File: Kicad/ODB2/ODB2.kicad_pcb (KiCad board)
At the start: 4 copper layers, 83.9 x 76.5 mm, 184 parts, among them J4 RF2-04A-T-00-50-G, J5 RFM_Conn_Coaxial, U1 STM32F412ZGTx, U10 W25Q512JVEIQ, U5 L76L-M33, U6 ICM-20948, U7 MS580301BA01-00

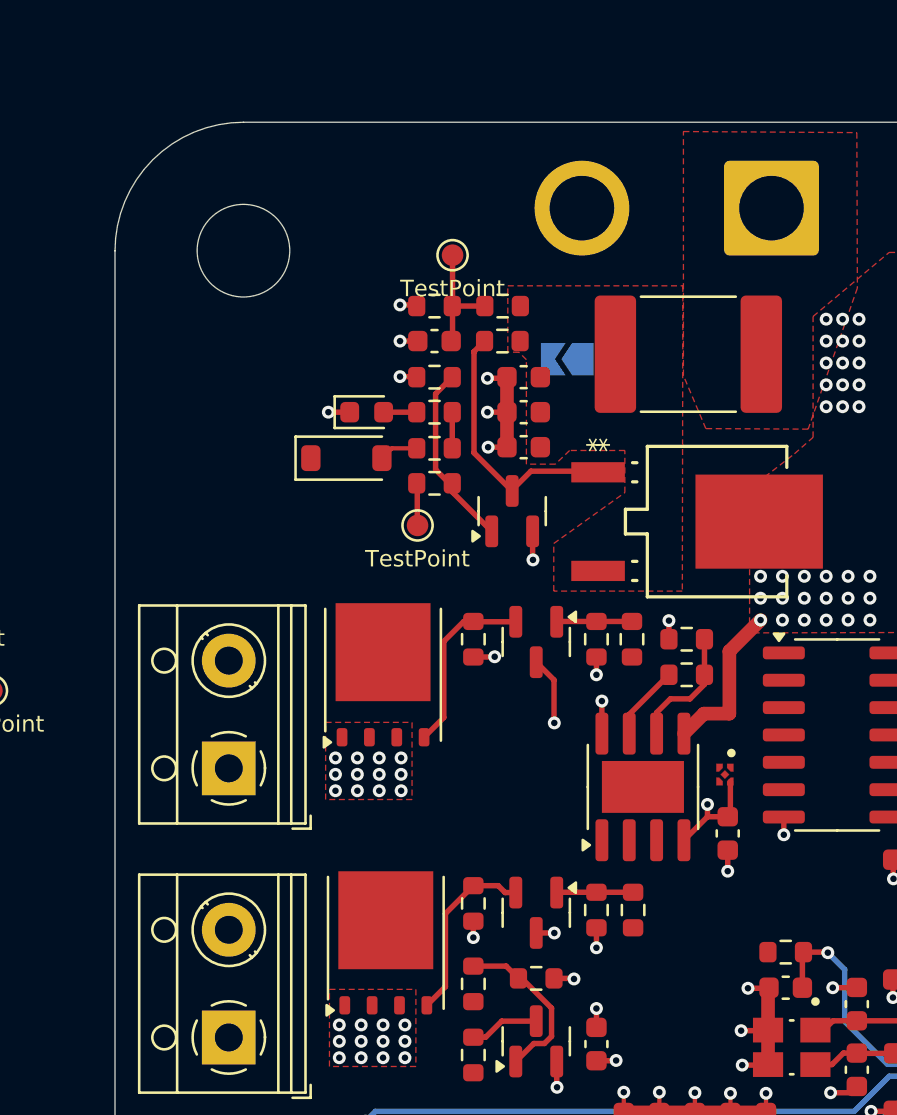
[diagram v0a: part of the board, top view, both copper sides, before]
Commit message: Changed XNOR Gate and OP AMP to 1 chanel
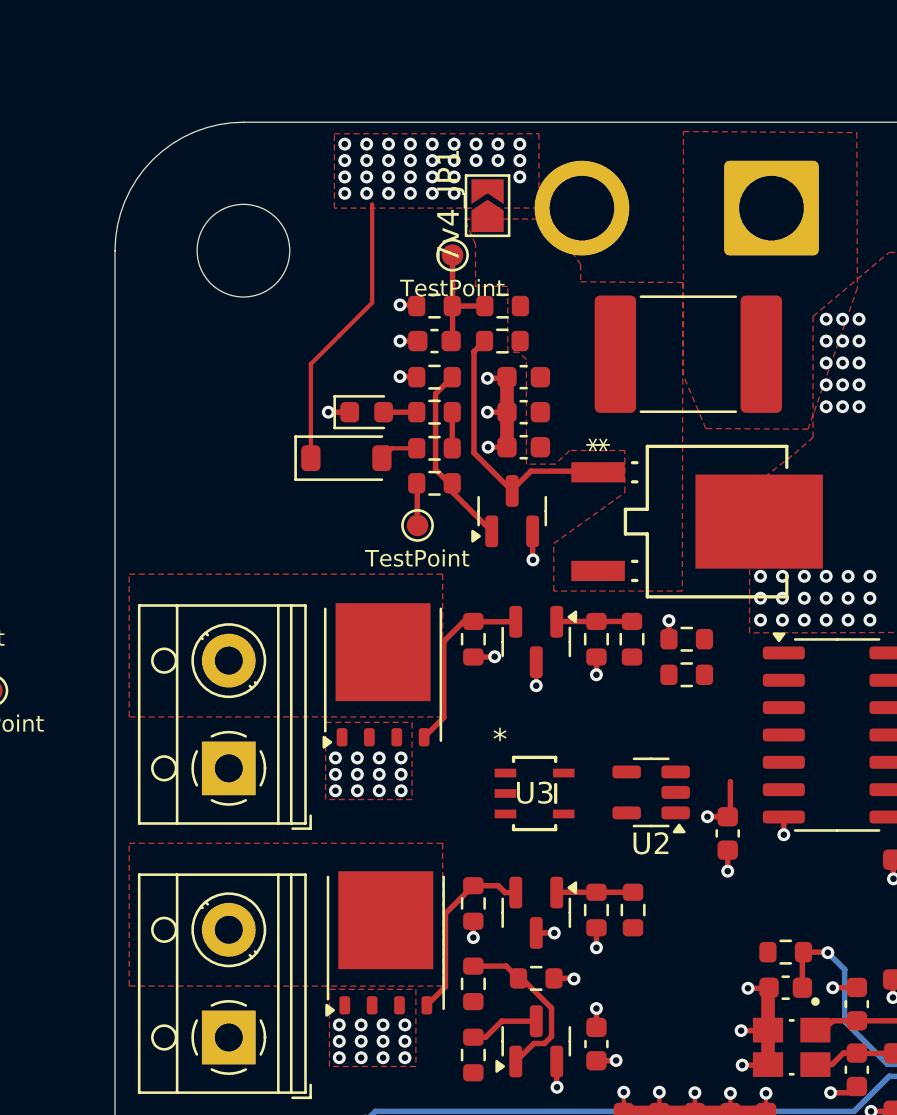
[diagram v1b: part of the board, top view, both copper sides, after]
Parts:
- removed Pyros_AMP1: TLV2372, Package_SO:SOIC-8-1EP_3.9x4.9mm_P1.27mm_EP2.41x3.81mm
- removed Pyros_XNOR1: 74LV1T87GXH, Library:IC_74LV1T87GXH
- added U2: TLV2371DBV, Package_TO_SOT_SMD:SOT-23-5, F.Cu at (24.9, 31.1)
- added U3: 74LV1T87GVH, ODB:SC-74A_SOT753_NEX, F.Cu at (19.5, 31.2)
- 7v4_JP1: moved to F.Cu
- moved 7v4_JP1 8.03 mm to (17.3, 3.87), turned to 90 degrees
- turned Pyros_R4 to 180 degrees
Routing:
- net Net-(U2--): track 5.84 -> 0.00 mm
- net +7V4: track 7.44 -> 13.0 mm, vias 33 -> 64
- net +3V3: track 103.2 -> 99.0 mm
- net Pyros_MainADC: track 3.49 -> 0.00 mm
- net GND: track 155.0 -> 153.4 mm, vias 150 -> 149
- added copper zone on F.Cu, net Net-(Pyros_J1-Pin_2)
- added copper zone on F.Cu, net Net-(Pyros_J2-Pin_2)

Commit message: Updated pcb
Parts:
- removed TP16: TestPoint, TestPoint:TestPoint_Pad_D1.0mm
- Boot_JP1: moved to F.Cu
- moved TP23 45.4 mm to (33.2, 34.2)
- moved TP15 34.6 mm to (28.9, 25.8)
- moved TP22 29.8 mm to (18.0, 33.6)
- moved TP12 27.4 mm to (14.6, 46.2)
- moved TP8 16.4 mm to (72.3, 27.0)
- moved TP7 16.1 mm to (74.6, 27.1)
- moved U3 7.99 mm to (27.1, 28.8)
- moved U2 3.71 mm to (22.0, 28.8)
- moved J5 1.57 mm to (18.5, 69.0)
- moved J4 1.39 mm to (79.3, 43.9)
- moved TP4 0.71 mm to (25.7, 54.8)
- moved Boot_JP1 0.67 mm to (45.2, 24.9)
- moved TP31 0.66 mm to (54.5, 6.88)
- moved TP3 0.61 mm to (23.4, 54.8)
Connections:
- U1 pad 45: Pyros_DrogueADC -> unconnected-(U1-PC5-Pad45)
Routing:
- net Pyros_MainOn: track 0.00 -> 93.1 mm, vias 0 -> 3
- net 7v4_An: track 5.54 -> 58.9 mm, vias 0 -> 2
- net Pyros_MainADC: track 0.00 -> 46.8 mm, vias 0 -> 4
- net 7v4Enable: track 1.96 -> 44.9 mm, vias 0 -> 3
- net SPI5_Mem_MOSI: track 1.92 -> 42.9 mm, vias 0 -> 2
- net Buzzer_PWM: track 0.00 -> 40.6 mm
- net ~Pyros_Test: track 0.00 -> 39.5 mm, vias 0 -> 4
- net SPI4_Baro_CS: track 4.19 -> 36.0 mm, vias 0 -> 2
- net SPI5_Mem_MISO: track 3.23 -> 30.8 mm, vias 0 -> 2
- net ICM_INT: track 3.66 -> 28.7 mm, vias 2 -> 3
- net Pyros_DrogueOn: track 0.00 -> 24.6 mm
- net Pyros_Bluetooth: track 0.00 -> 24.2 mm
- net Pyros_DrogueODB: track 0.00 -> 21.9 mm, vias 0 -> 2
- net +7V4: track 13.0 -> 34.3 mm
- net Pyros_MainODB: track 0.00 -> 20.0 mm, vias 0 -> 2
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
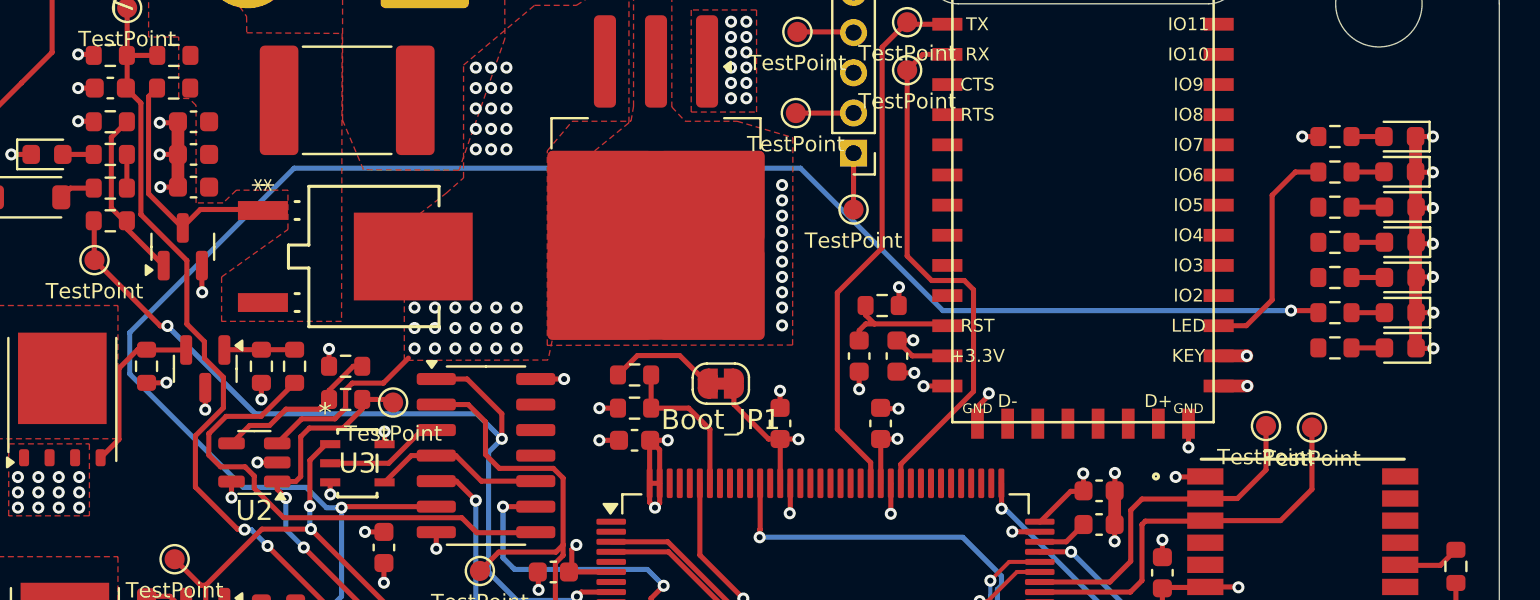
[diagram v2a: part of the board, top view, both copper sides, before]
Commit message: pcb fixes leds
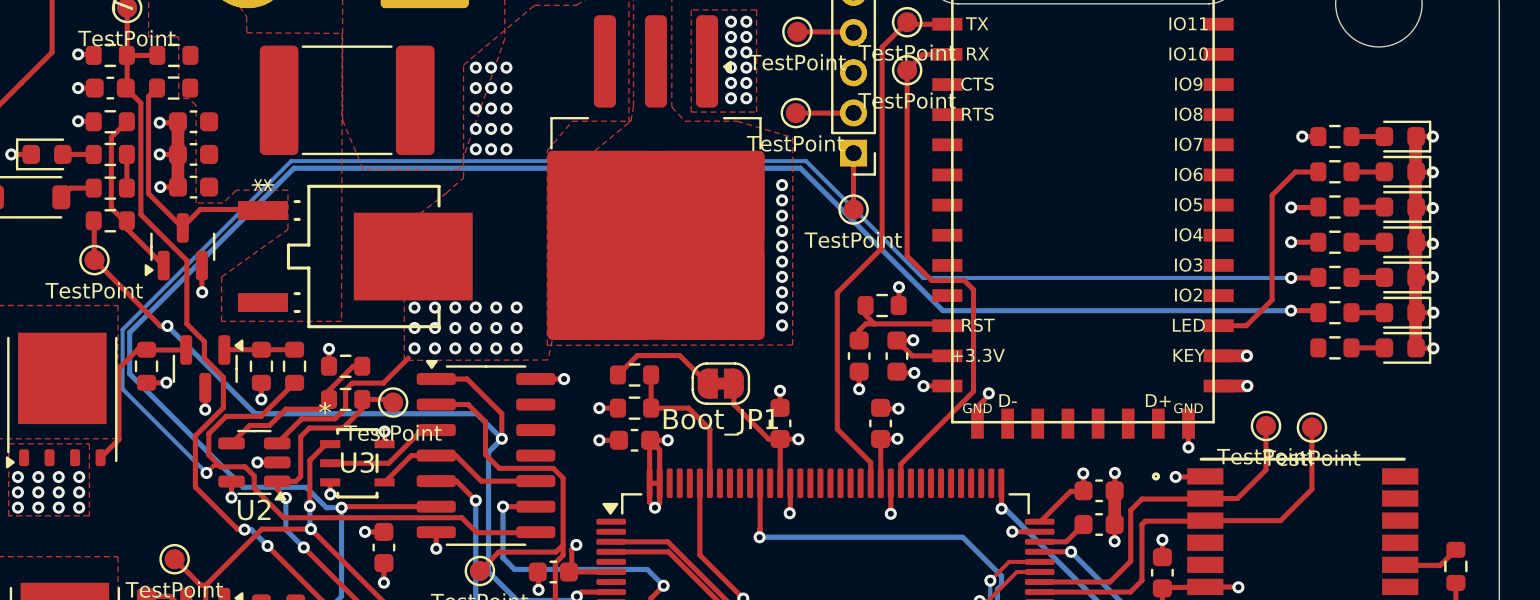
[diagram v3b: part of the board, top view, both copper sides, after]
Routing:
- net Pyros_DrogueOn: track 24.6 -> 99.6 mm, vias 0 -> 2
- net 7v4Enable: track 44.9 -> 46.2 mm, vias 3 -> 4
- net Pyros_Bluetooth: track 24.2 -> 25.4 mm, vias 0 -> 1
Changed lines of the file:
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@@
 		(tags "net tie solder jumper bridged")
 		(property "Reference" "Boot_JP1"
-			(at 0 -1.8 360)
+			(at 0 -1.8 0)
 			(layer "F.SilkS")
 			(effects
@@
 		)
 		(property "Value" "SolderJumper_2_Open"
-			(at 0 1.9 360)
+			(at 0 1.9 0)
 			(layer "F.Fab")
 			(effects
@@
 	(footprint "LED_SMD:LED_0603_1608Metric"
 		(layer "F.Cu")
-		(at 78.9941 14.3256 180)
+		(at 79.0194 14.3256 180)
 		(descr "LED SMD 0603 (1608 Metric), square (rectangular) end terminal, IPC_7351 nominal, (Body size source: http://www.tortai-tech.com/upload/download/2011102023233369053.pdf), generated with kicad-footprint-generator")
 		(tags "LED")
@@
 	(footprint "Resistor_SMD:R_0603_1608Metric"
 		(layer "F.Cu")
-		(at 75.7683 21.336 180)
+		(at 75.7682 21.336 180)
 		(descr "Resistor SMD 0603 (1608 Metric), square (rectangular) end terminal, IPC_7351 nominal, (Body size source: IPC-SM-782 page 72, https://www.pcb-3d.com/wordpress/wp-content/uploads/ipc-sm-782a_amendment_1_and_2.pdf), generated with kicad-footprint-generator")
 		(tags "resistor")
@@
 	(footprint "LED_SMD:LED_0603_1608Metric"
 		(layer "F.Cu")
-		(at 79.0195 16.0782 180)
+		(at 79.0194 16.0782 180)
 		(descr "LED SMD 0603 (1608 Metric), square (rectangular) end terminal, IPC_7351 nominal, (Body size source: http://www.tortai-tech.com/upload/download/2011102023233369053.pdf), generated with kicad-footprint-generator")
 		(tags "LED")
@@
 	(footprint "LED_SMD:LED_0603_1608Metric"
 		(layer "F.Cu")
-		(at 78.9941 12.573 180)
+		(at 79.0194 12.573 180)
 		(descr "LED SMD 0603 (1608 Metric), square (rectangular) end terminal, IPC_7351 nominal, (Body size source: http://www.tortai-tech.com/upload/download/2011102023233369053.pdf), generated with kicad-footprint-generator")
 		(tags "LED")
@@
 	(footprint "Resistor_SMD:R_0603_1608Metric"
 		(layer "F.Cu")
-		(at 75.7683 16.087)
+		(at 75.7682 16.0782)
 		(descr "Resistor SMD 0603 (1608 Metric), square (rectangular) end terminal, IPC_7351 nominal, (Body size source: IPC-SM-782 page 72, https://www.pcb-3d.com/wordpress/wp-content/uploads/ipc-sm-782a_amendment_1_and_2.pdf), generated with kicad-footprint-generator")
 		(tags "resistor")
@@
 	(footprint "LED_SMD:LED_0603_1608Metric"
 		(layer "F.Cu")
-		(at 79.0195 17.8308 180)
+		(at 79.0194 17.8308 180)
 		(descr "LED SMD 0603 (1608 Metric), square (rectangular) end terminal, IPC_7351 nominal, (Body size source: http://www.tortai-tech.com/upload/download/2011102023233369053.pdf), generated with kicad-footprint-generator")
 		(tags "LED")
@@
 	(footprint "Resistor_SMD:R_0603_1608Metric"
 		(layer "F.Cu")
-		(at 75.7683 23.0886 180)
+		(at 75.7682 23.0886 180)
 		(descr "Resistor SMD 0603 (1608 Metric), square (rectangular) end terminal, IPC_7351 nominal, (Body size source: IPC-SM-782 page 72, https://www.pcb-3d.com/wordpress/wp-content/uploads/ipc-sm-782a_amendment_1_and_2.pdf), generated with kicad-footprint-generator")
 		(tags "resistor")
@@
 	(footprint "Resistor_SMD:R_0603_1608Metric"
 		(layer "F.Cu")
-		(at 75.7683 14.337)
+		(at 75.7682 14.3256)
 		(descr "Resistor SMD 0603 (1608 Metric), square (rectangular) end terminal, IPC_7351 nominal, (Body size source: IPC-SM-782 page 72, https://www.pcb-3d.com/wordpress/wp-content/uploads/ipc-sm-782a_amendment_1_and_2.pdf), generated with kicad-footprint-generator")
 		(tags "resistor")
@@
 	(footprint "Resistor_SMD:R_0603_1608Metric"
 		(layer "F.Cu")
-		(at 75.7683 19.587 180)
+		(at 75.7682 19.5834 180)
 		(descr "Resistor SMD 0603 (1608 Metric), square (rectangular) end terminal, IPC_7351 nominal, (Body size source: IPC-SM-782 page 72, https://www.pcb-3d.com/wordpress/wp-content/uploads/ipc-sm-782a_amendment_1_and_2.pdf), generated with kicad-footprint-generator")
 		(tags "resistor")
@@
 	(footprint "LED_SMD:LED_0603_1608Metric"
 		(layer "F.Cu")
-		(at 79.0195 21.336 180)
+		(at 79.0194 21.336 180)
 		(descr "LED SMD 0603 (1608 Metric), square (rectangular) end terminal, IPC_7351 nominal, (Body size source: http://www.tortai-tech.com/upload/download/2011102023233369053.pdf), generated with kicad-footprint-generator")
 		(tags "LED")
@@
 	(footprint "Resistor_SMD:R_0603_1608Metric"
 		(layer "F.Cu")
-		(at 75.7683 17.837 180)
+		(at 75.7682 17.8308 180)
 		(descr "Resistor SMD 0603 (1608 Metric), square (rectangular) end terminal, IPC_7351 nominal, (Body size source: IPC-SM-782 page 72, https://www.pcb-3d.com/wordpress/wp-content/uploads/ipc-sm-782a_amendment_1_and_2.pdf), generated with kicad-footprint-generator")
 		(tags "resistor")
@@
 	(footprint "LED_SMD:LED_0603_1608Metric"
 		(layer "F.Cu")
-		(at 79.0195 23.0886 180)
+		(at 79.0194 23.0886 180)
 		(descr "LED SMD 0603 (1608 Metric), square (rectangular) end terminal, IPC_7351 nominal, (Body size source: http://www.tortai-tech.com/upload/download/2011102023233369053.pdf), generated with kicad-footprint-generator")
 		(tags "LED")
@@
 	(footprint "LED_SMD:LED_0603_1608Metric"
 		(layer "F.Cu")
-		(at 79.0195 19.5834 180)
+		(at 79.0194 19.5834 180)
 		(descr "LED SMD 0603 (1608 Metric), square (rectangular) end terminal, IPC_7351 nominal, (Body size source: http://www.tortai-tech.com/upload/download/2011102023233369053.pdf), generated with kicad-footprint-generator")
 		(tags "LED")
@@
 	(footprint "Resistor_SMD:R_0603_1608Metric"
 		(layer "F.Cu")
-		(at 75.7683 12.573)
+		(at 75.7682 12.573)
 		(descr "Resistor SMD 0603 (1608 Metric), square (rectangular) end terminal, IPC_7351 nominal, (Body size source: IPC-SM-782 page 72, https://www.pcb-3d.com/wordpress/wp-content/uploads/ipc-sm-782a_amendment_1_and_2.pdf), generated with kicad-footprint-generator")
 		(tags "resistor")
@@
 	)
 	(segment
+		(start 73.58985 16.1036)
+		(end 74.84775 16.1036)
+		(width 0.254)
+		(layer "F.Cu")
+		(net 23)
+	)
+	(segment
 		(start 38.270001 35.237599)
 		(end 38.0492 35.4584)
@@
 	)
 	(via
+		(at 73.58985 16.1036)
+		(size 0.6)
+		(drill 0.3)
+		(layers "F.Cu" "B.Cu")
+		(net 23)
+	)
+	(via
 		(at 38.0492 35.4584)
 		(size 0.6)
@@
 	)
 	(segment
+		(start 73.58985 17.8308)
+		(end 74.84775 17.8308)
+		(width 0.254)
+		(layer "F.Cu")
+		(net 80)
+	)
+	(segment
 		(start 36.9788 37.0804)
 		(end 37.636 37.7376)
@@
 		(net 80)
 	)
+	(via
+		(at 73.58985 17.8308)
+		(size 0.6)
+		(drill 0.3)
+		(layers "F.Cu" "B.Cu")
+		(net 80)
+	)
 	(segment
 		(start 36.003 30.988)
@@
 	)
 	(segment
+		(start 73.58985 19.6088)
+		(end 74.84775 19.6088)
+		(width 0.254)
+		(layer "F.Cu")
+		(net 84)
+	)
+	(segment
+		(start 20.2692 28.956)
+		(end 19.97787 28.956)
+		(width 0.2)
+		(layer "F.Cu")
+		(net 84)
+	)
+	(segment
 		(start 32.322877 31.539776)
 		(end 33.066501 32.2834)
@@
 	)
 	(segment
+		(start 19.97787 28.956)
+		(end 19.62227 29.3116)
+		(width 0.2)
+		(layer "F.Cu")
+		(net 84)
+	)
+	(segment
 		(start 20.32 29.0068)
 		(end 21.5392 29.0068)
@@
 	)
 	(segment
+		(start 20.32 29.0068)
+		(end 20.2692 28.956)
+		(width 0.2)
+		(layer "F.Cu")
+		(net 84)
+	)
+	(segment
 		(start 24.003 24.828)
 		(end 22.3356 26.4954)
@@
 		(net 84)
 	)
+	(via
+		(at 19.62227 29.3116)
+		(size 0.6)
+		(drill 0.3)
+		(layers "F.Cu" "B.Cu")
+		(net 84)
+	)
+	(via
+		(at 73.58985 19.6088)
+		(size 0.6)
+		(drill 0.3)
+		(layers "F.Cu" "B.Cu")
+		(net 84)
+	)
+	(segment
+		(start 23.830968 13.7938)
+		(end 49.4538 13.7938)
+		(width 0.2)
+		(layer "B.Cu")
+		(net 84)
+	)
+	(segment
+		(start 49.4538 13.7938)
+		(end 55.2688 19.6088)
+		(width 0.2)
+		(layer "B.Cu")
+		(net 84)
+	)
+	(segment
+		(start 15.4448 25.13413)
+		(end 15.4448 22.179968)
+		(width 0.2)
+		(layer "B.Cu")
+		(net 84)
+	)
+	(segment
+		(start 19.62227 29.3116)
+		(end 15.4448 25.13413)
+		(width 0.2)
+		(layer "B.Cu")
+		(net 84)
+	)
+	(segment
+		(start 15.4448 22.179968)
+		(end 23.830968 13.7938)
+		(width 0.2)
+		(layer "B.Cu")
+		(net 84)
+	)
+	(segment
+		(start 55.2688 19.6088)
+		(end 73.58985 19.6088)
+		(width 0.2)
+		(layer "B.Cu")
+		(net 84)
+	)
